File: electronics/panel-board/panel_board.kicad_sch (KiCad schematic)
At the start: 0 parts

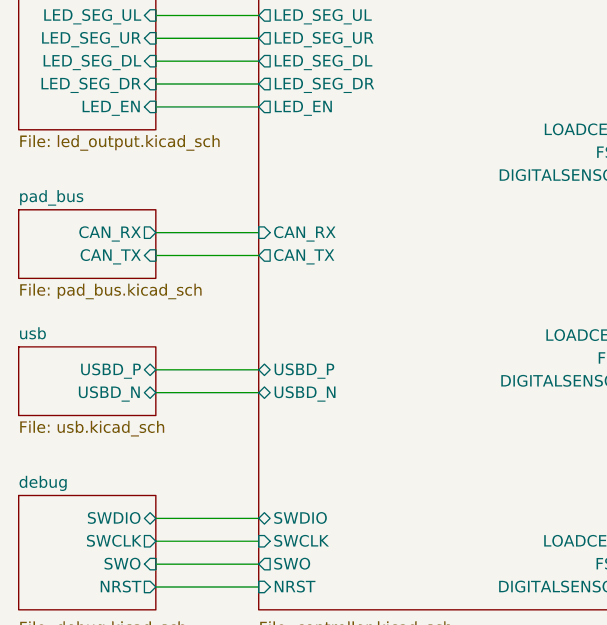
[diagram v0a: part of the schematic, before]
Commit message: Update PadBUS standard
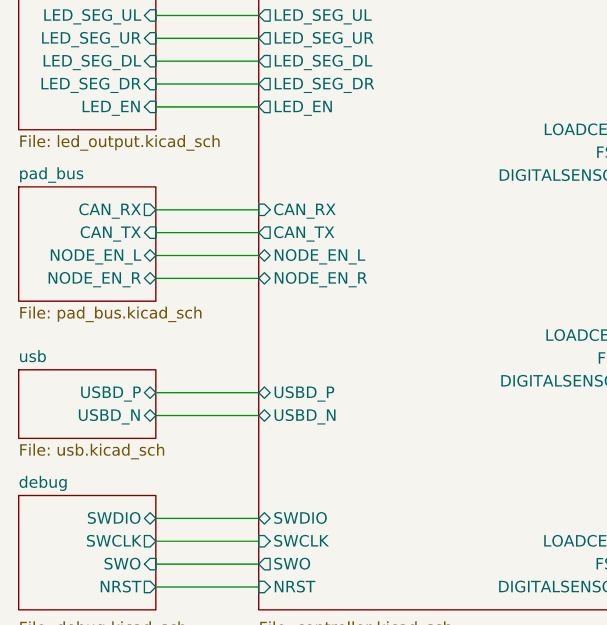
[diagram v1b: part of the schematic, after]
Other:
- sheet controller ports: added NODE_EN_L, NODE_EN_R; removed none
- sheet pad_bus ports: added NODE_EN_L, NODE_EN_R; removed none
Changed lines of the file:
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@@
     (stroke (width 0) (type default) (color 0 0 0 0))
   )
-  (wire (pts (xy 100.33 101.6) (xy 111.76 101.6))
+  (wire (pts (xy 100.33 104.14) (xy 111.76 104.14))
     (stroke (width 0) (type default) (color 0 0 0 0))
   )
@@
     (stroke (width 0) (type default) (color 0 0 0 0))
   )
+  (wire (pts (xy 100.33 86.36) (xy 111.76 86.36))
+    (stroke (width 0) (type default) (color 0 0 0 0))
+  )
+  (wire (pts (xy 157.48 77.47) (xy 168.91 77.47))
+    (stroke (width 0) (type default) (color 0 0 0 0))
+  )
+  (wire (pts (xy 157.48 74.93) (xy 168.91 74.93))
+    (stroke (width 0) (type default) (color 0 0 0 0))
+  )
+  (wire (pts (xy 100.33 118.11) (xy 111.76 118.11))
+    (stroke (width 0) (type default) (color 0 0 0 0))
+  )
+  (wire (pts (xy 100.33 106.68) (xy 111.76 106.68))
+    (stroke (width 0) (type default) (color 0 0 0 0))
+  )
+  (wire (pts (xy 157.48 120.65) (xy 168.91 120.65))
+    (stroke (width 0) (type default) (color 0 0 0 0))
+  )
+  (wire (pts (xy 157.48 102.87) (xy 168.91 102.87))
+    (stroke (width 0) (type default) (color 0 0 0 0))
+  )
+  (wire (pts (xy 157.48 100.33) (xy 168.91 100.33))
+    (stroke (width 0) (type default) (color 0 0 0 0))
+  )
+  (wire (pts (xy 100.33 64.77) (xy 111.76 64.77))
+    (stroke (width 0) (type default) (color 0 0 0 0))
+  )
+  (wire (pts (xy 157.48 52.07) (xy 168.91 52.07))
+    (stroke (width 0) (type default) (color 0 0 0 0))
+  )
+  (wire (pts (xy 157.48 97.79) (xy 168.91 97.79))
+    (stroke (width 0) (type default) (color 0 0 0 0))
+  )
+  (wire (pts (xy 157.48 80.01) (xy 168.91 80.01))
+    (stroke (width 0) (type default) (color 0 0 0 0))
+  )
+  (wire (pts (xy 157.48 54.61) (xy 168.91 54.61))
+    (stroke (width 0) (type default) (color 0 0 0 0))
+  )
+  (wire (pts (xy 100.33 125.73) (xy 111.76 125.73))
+    (stroke (width 0) (type default) (color 0 0 0 0))
+  )
+  (wire (pts (xy 157.48 125.73) (xy 168.91 125.73))
+    (stroke (width 0) (type default) (color 0 0 0 0))
+  )
+  (wire (pts (xy 100.33 83.82) (xy 111.76 83.82))
+    (stroke (width 0) (type default) (color 0 0 0 0))
+  )
   (wire (pts (xy 100.33 88.9) (xy 111.76 88.9))
     (stroke (width 0) (type default) (color 0 0 0 0))
   )
-  (wire (pts (xy 157.48 77.47) (xy 168.91 77.47))
-    (stroke (width 0) (type default) (color 0 0 0 0))
-  )
-  (wire (pts (xy 157.48 74.93) (xy 168.91 74.93))
-    (stroke (width 0) (type default) (color 0 0 0 0))
-  )
-  (wire (pts (xy 100.33 118.11) (xy 111.76 118.11))
-    (stroke (width 0) (type default) (color 0 0 0 0))
-  )
-  (wire (pts (xy 100.33 104.14) (xy 111.76 104.14))
-    (stroke (width 0) (type default) (color 0 0 0 0))
-  )
-  (wire (pts (xy 157.48 120.65) (xy 168.91 120.65))
-    (stroke (width 0) (type default) (color 0 0 0 0))
-  )
-  (wire (pts (xy 157.48 102.87) (xy 168.91 102.87))
-    (stroke (width 0) (type default) (color 0 0 0 0))
-  )
-  (wire (pts (xy 157.48 100.33) (xy 168.91 100.33))
-    (stroke (width 0) (type default) (color 0 0 0 0))
-  )
-  (wire (pts (xy 100.33 64.77) (xy 111.76 64.77))
-    (stroke (width 0) (type default) (color 0 0 0 0))
-  )
-  (wire (pts (xy 157.48 52.07) (xy 168.91 52.07))
-    (stroke (width 0) (type default) (color 0 0 0 0))
-  )
-  (wire (pts (xy 157.48 97.79) (xy 168.91 97.79))
-    (stroke (width 0) (type default) (color 0 0 0 0))
-  )
-  (wire (pts (xy 157.48 80.01) (xy 168.91 80.01))
-    (stroke (width 0) (type default) (color 0 0 0 0))
-  )
-  (wire (pts (xy 157.48 54.61) (xy 168.91 54.61))
-    (stroke (width 0) (type default) (color 0 0 0 0))
-  )
-  (wire (pts (xy 100.33 125.73) (xy 111.76 125.73))
-    (stroke (width 0) (type default) (color 0 0 0 0))
-  )
-  (wire (pts (xy 157.48 125.73) (xy 168.91 125.73))
-    (stroke (width 0) (type default) (color 0 0 0 0))
-  )
-  (wire (pts (xy 100.33 86.36) (xy 111.76 86.36))
+  (wire (pts (xy 100.33 91.44) (xy 111.76 91.44))
     (stroke (width 0) (type default) (color 0 0 0 0))
   )
@@
       (effects (font (size 1.27 1.27)) (justify left))
     )
-    (pin "CAN_TX" output (at 111.76 88.9 180)
-      (effects (font (size 1.27 1.27)) (justify left))
-    )
-    (pin "CAN_RX" input (at 111.76 86.36 180)
+    (pin "CAN_TX" output (at 111.76 86.36 180)
+      (effects (font (size 1.27 1.27)) (justify left))
+    )
+    (pin "CAN_RX" input (at 111.76 83.82 180)
       (effects (font (size 1.27 1.27)) (justify left))
     )
@@
       (effects (font (size 1.27 1.27)) (justify left))
     )
-    (pin "USBD_P" bidirectional (at 111.76 101.6 180)
-      (effects (font (size 1.27 1.27)) (justify left))
-    )
-    (pin "USBD_N" bidirectional (at 111.76 104.14 180)
+    (pin "USBD_P" bidirectional (at 111.76 104.14 180)
+      (effects (font (size 1.27 1.27)) (justify left))
+    )
+    (pin "USBD_N" bidirectional (at 111.76 106.68 180)
       (effects (font (size 1.27 1.27)) (justify left))
     )
@@
       (effects (font (size 1.27 1.27)) (justify left))
     )
-  )
-  (sheet (at 85.09 99.06) (size 15.24 7.62) (fields_autoplaced)
-    (stroke (width 0.1524) (type solid) (color 0 0 0 0))
-    (fill (color 0 0 0 0.0000))
-    (property "Sheet name" "usb" (id 0) (at 85.09 98.3484 0)
-      (effects (font (size 1.27 1.27)) (justify left bottom))
-    )
-    (property "Sheet file" "usb.kicad_sch" (id 1) (at 85.09 107.2646 0)
-      (effects (font (size 1.27 1.27)) (justify left top))
-    )
-    (pin "USBD_P" bidirectional (at 100.33 101.6 0)
-      (effects (font (size 1.27 1.27)) (justify right))
-    )
-    (pin "USBD_N" bidirectional (at 100.33 104.14 0)
+    (pin "NODE_EN_L" bidirectional (at 111.76 88.9 180)
+      (effects (font (size 1.27 1.27)) (justify left))
+    )
+    (pin "NODE_EN_R" bidirectional (at 111.76 91.44 180)
+      (effects (font (size 1.27 1.27)) (justify left))
+    )
+  )
+  (sheet (at 85.09 101.6) (size 15.24 7.62) (fields_autoplaced)
+    (stroke (width 0.1524) (type solid) (color 0 0 0 0))
+    (fill (color 0 0 0 0.0000))
+    (property "Sheet name" "usb" (id 0) (at 85.09 100.8884 0)
+      (effects (font (size 1.27 1.27)) (justify left bottom))
+    )
+    (property "Sheet file" "usb.kicad_sch" (id 1) (at 85.09 109.8046 0)
+      (effects (font (size 1.27 1.27)) (justify left top))
+    )
+    (pin "USBD_P" bidirectional (at 100.33 104.14 0)
+      (effects (font (size 1.27 1.27)) (justify right))
+    )
+    (pin "USBD_N" bidirectional (at 100.33 106.68 0)
       (effects (font (size 1.27 1.27)) (justify right))
     )
@@
     )
   )
-  (sheet (at 85.09 83.82) (size 15.24 7.62) (fields_autoplaced)
-    (stroke (width 0.1524) (type solid) (color 0 0 0 0))
-    (fill (color 0 0 0 0.0000))
-    (property "Sheet name" "pad_bus" (id 0) (at 85.09 83.1084 0)
-      (effects (font (size 1.27 1.27)) (justify left bottom))
-    )
-    (property "Sheet file" "pad_bus.kicad_sch" (id 1) (at 85.09 92.0246 0)
-      (effects (font (size 1.27 1.27)) (justify left top))
-    )
-    (pin "CAN_RX" output (at 100.33 86.36 0)
-      (effects (font (size 1.27 1.27)) (justify right))
-    )
-    (pin "CAN_TX" input (at 100.33 88.9 0)
-      (effects (font (size 1.27 1.27)) (justify right))
-    )
+  (sheet (at 85.09 81.28) (size 15.24 12.7) (fields_autoplaced)
+    (stroke (width 0.1524) (type solid) (color 0 0 0 0))
+    (fill (color 0 0 0 0.0000))
+    (property "Sheet name" "pad_bus" (id 0) (at 85.09 80.5684 0)
+      (effects (font (size 1.27 1.27)) (justify left bottom))
+    )
+    (property "Sheet file" "pad_bus.kicad_sch" (id 1) (at 85.09 94.5646 0)
+      (effects (font (size 1.27 1.27)) (justify left top))
+    )
+    (pin "CAN_RX" output (at 100.33 83.82 0)
+      (effects (font (size 1.27 1.27)) (justify right))
+    )
+    (pin "CAN_TX" input (at 100.33 86.36 0)
+      (effects (font (size 1.27 1.27)) (justify right))
+    )
+    (pin "NODE_EN_R" bidirectional (at 100.33 91.44 0)
+      (effects (font (size 1.27 1.27)) (justify right))
+    )
+    (pin "NODE_EN_L" bidirectional (at 100.33 88.9 0)
+      (effects (font (size 1.27 1.27)) (justify right))
+    )

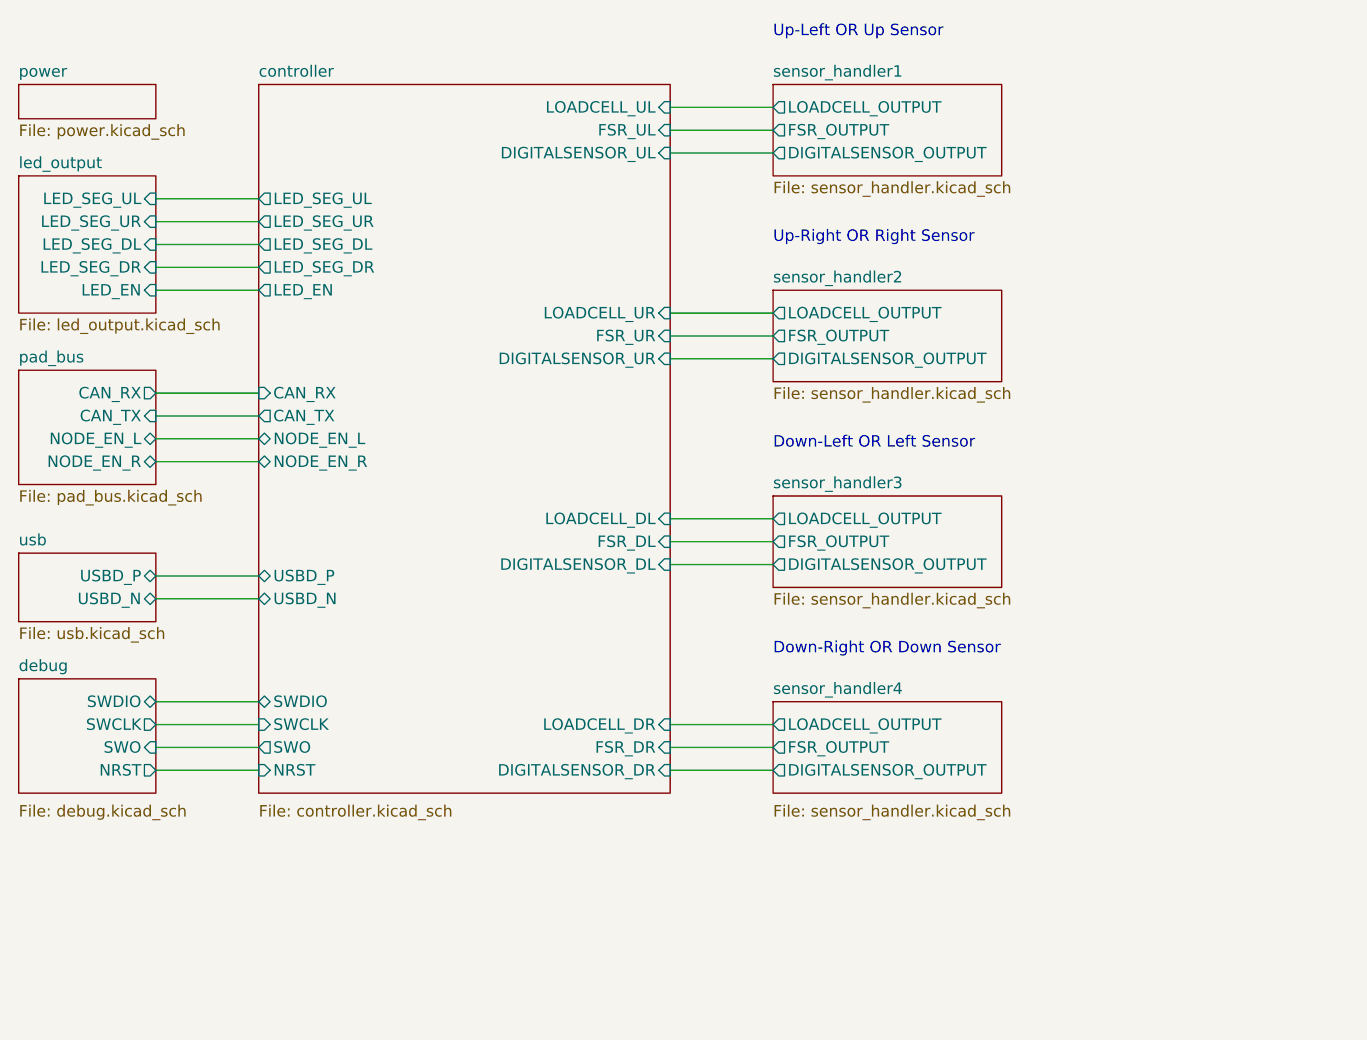
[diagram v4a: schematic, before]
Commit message: Prelim schematic for FSR+LC gain/adj dig control
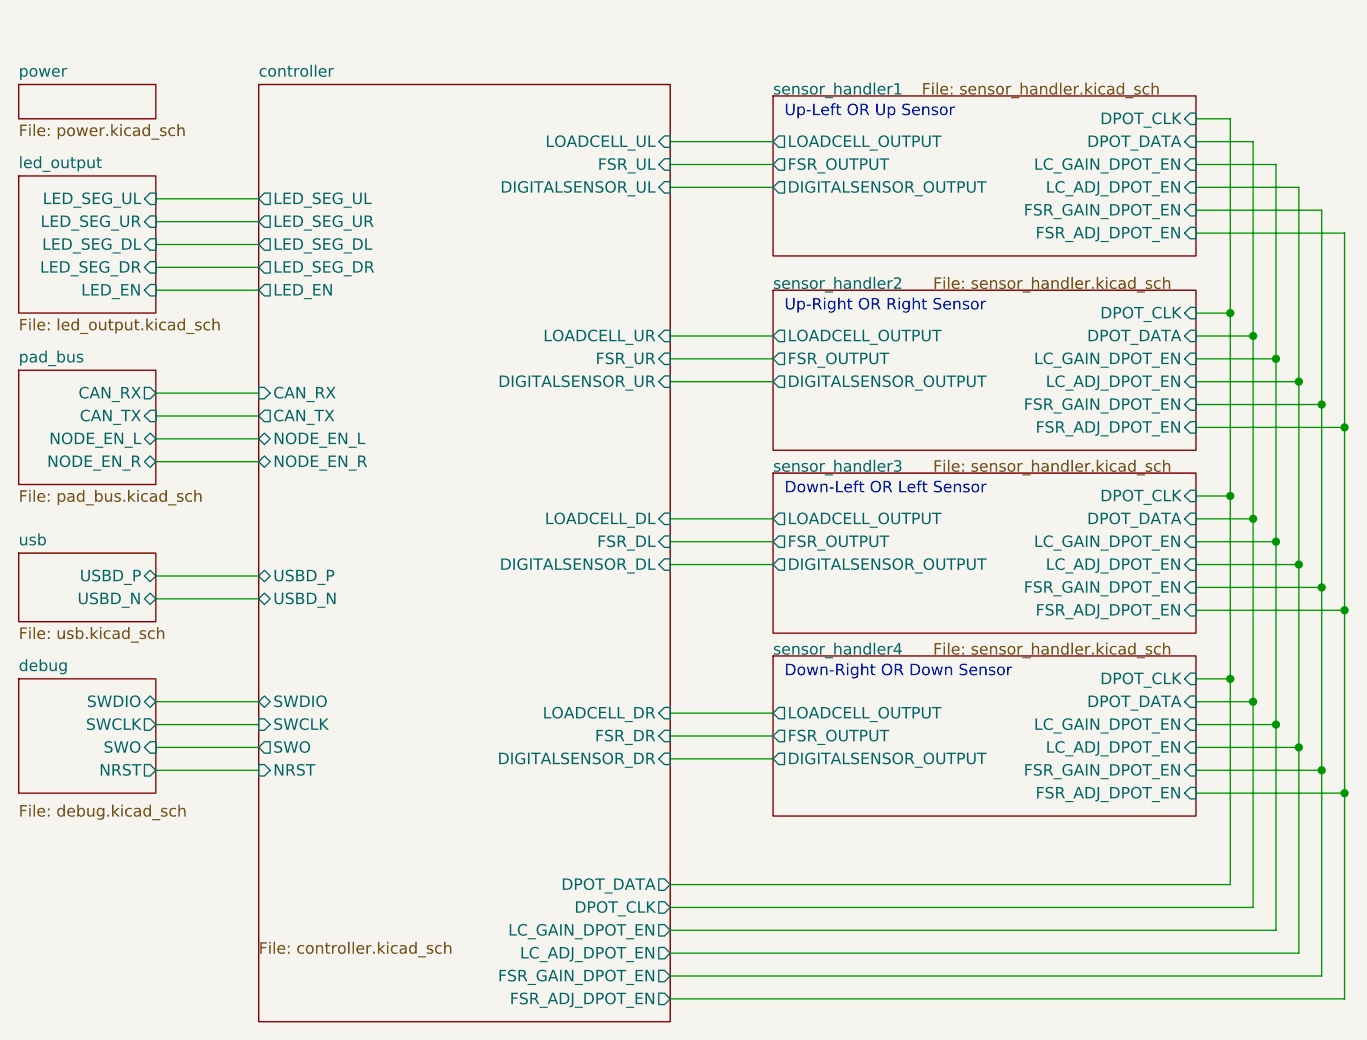
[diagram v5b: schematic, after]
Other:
- sheet controller ports: added DPOT_CLK, DPOT_DATA, FSR_ADJ_DPOT_EN, FSR_GAIN_DPOT_EN, LC_ADJ_DPOT_EN, LC_GAIN_DPOT_EN; removed none
- sheet sensor_handler1 ports: added DPOT_CLK, DPOT_DATA, FSR_ADJ_DPOT_EN, FSR_GAIN_DPOT_EN, LC_ADJ_DPOT_EN, LC_GAIN_DPOT_EN; removed none
- sheet sensor_handler2 ports: added DPOT_CLK, DPOT_DATA, FSR_ADJ_DPOT_EN, FSR_GAIN_DPOT_EN, LC_ADJ_DPOT_EN, LC_GAIN_DPOT_EN; removed none
- sheet sensor_handler3 ports: added DPOT_CLK, DPOT_DATA, FSR_ADJ_DPOT_EN, FSR_GAIN_DPOT_EN, LC_ADJ_DPOT_EN, LC_GAIN_DPOT_EN; removed none
- sheet sensor_handler4 ports: added DPOT_CLK, DPOT_DATA, FSR_ADJ_DPOT_EN, FSR_GAIN_DPOT_EN, LC_ADJ_DPOT_EN, LC_GAIN_DPOT_EN; removed none
